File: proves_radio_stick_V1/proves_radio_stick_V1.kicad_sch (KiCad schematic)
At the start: 60 parts, among them J1 SWD Port, J12 USB_C_Receptacle_USB2.0_16P, J2 Conn_Coaxial, J22 SWD Port, SW1 KMR2, SW2 KMR2, U11 W25Q128JVS, U18 RP2350_60QFN, U2 TPS62085RLTT, U3 E32-400M20S_C2965514, Y1 ABM8-272-T3

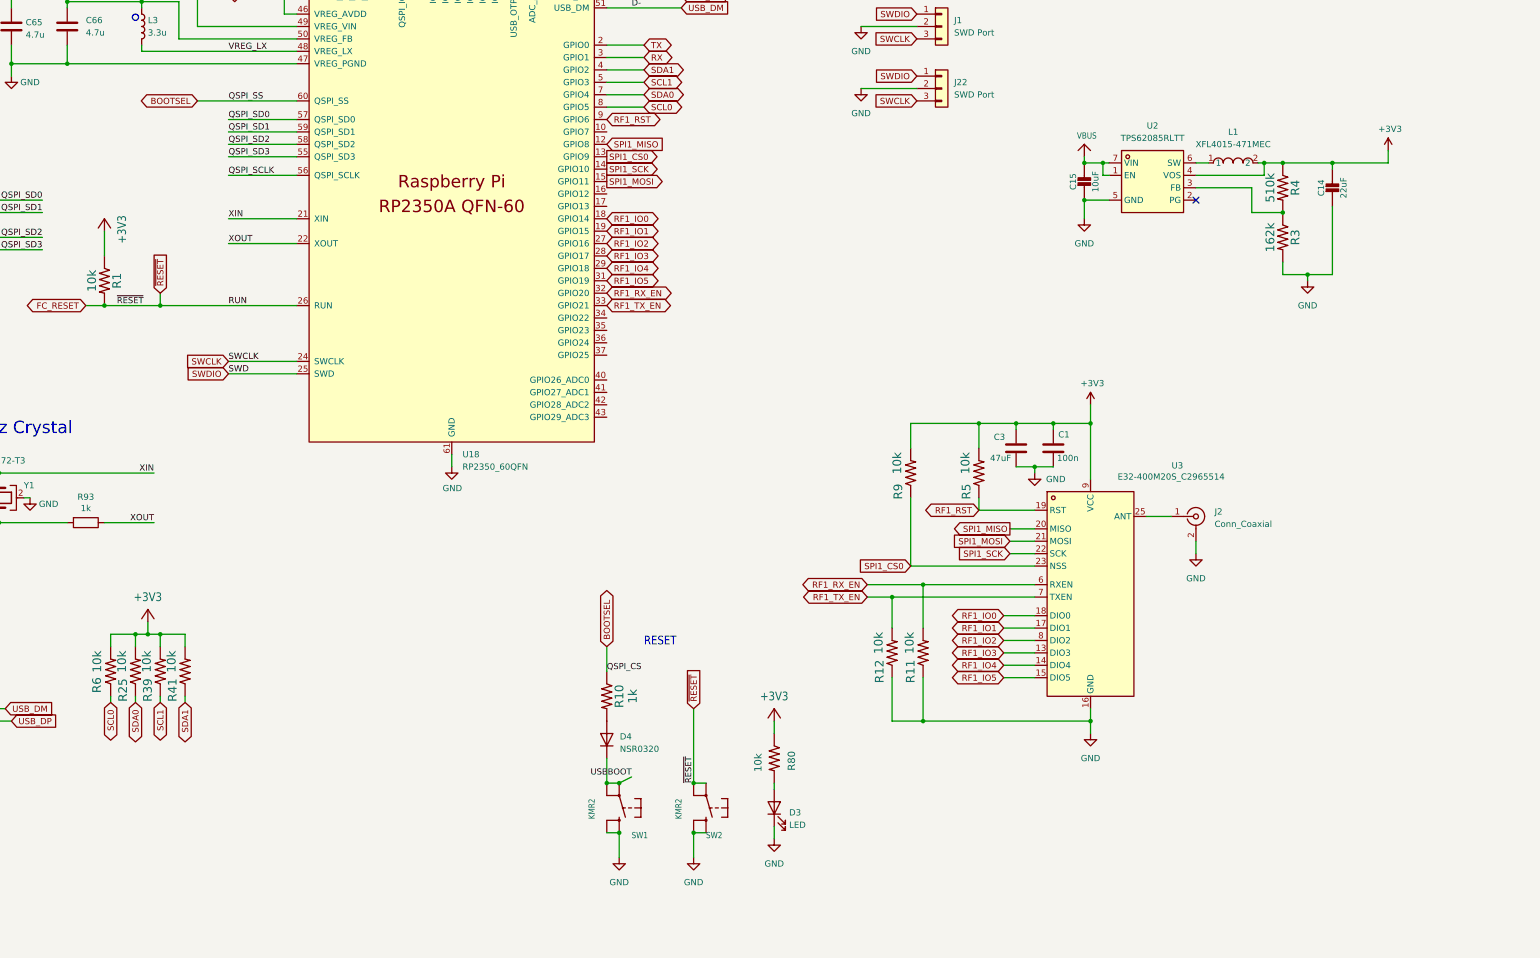
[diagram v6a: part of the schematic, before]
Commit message: Updated with Screw Terminals and Vias
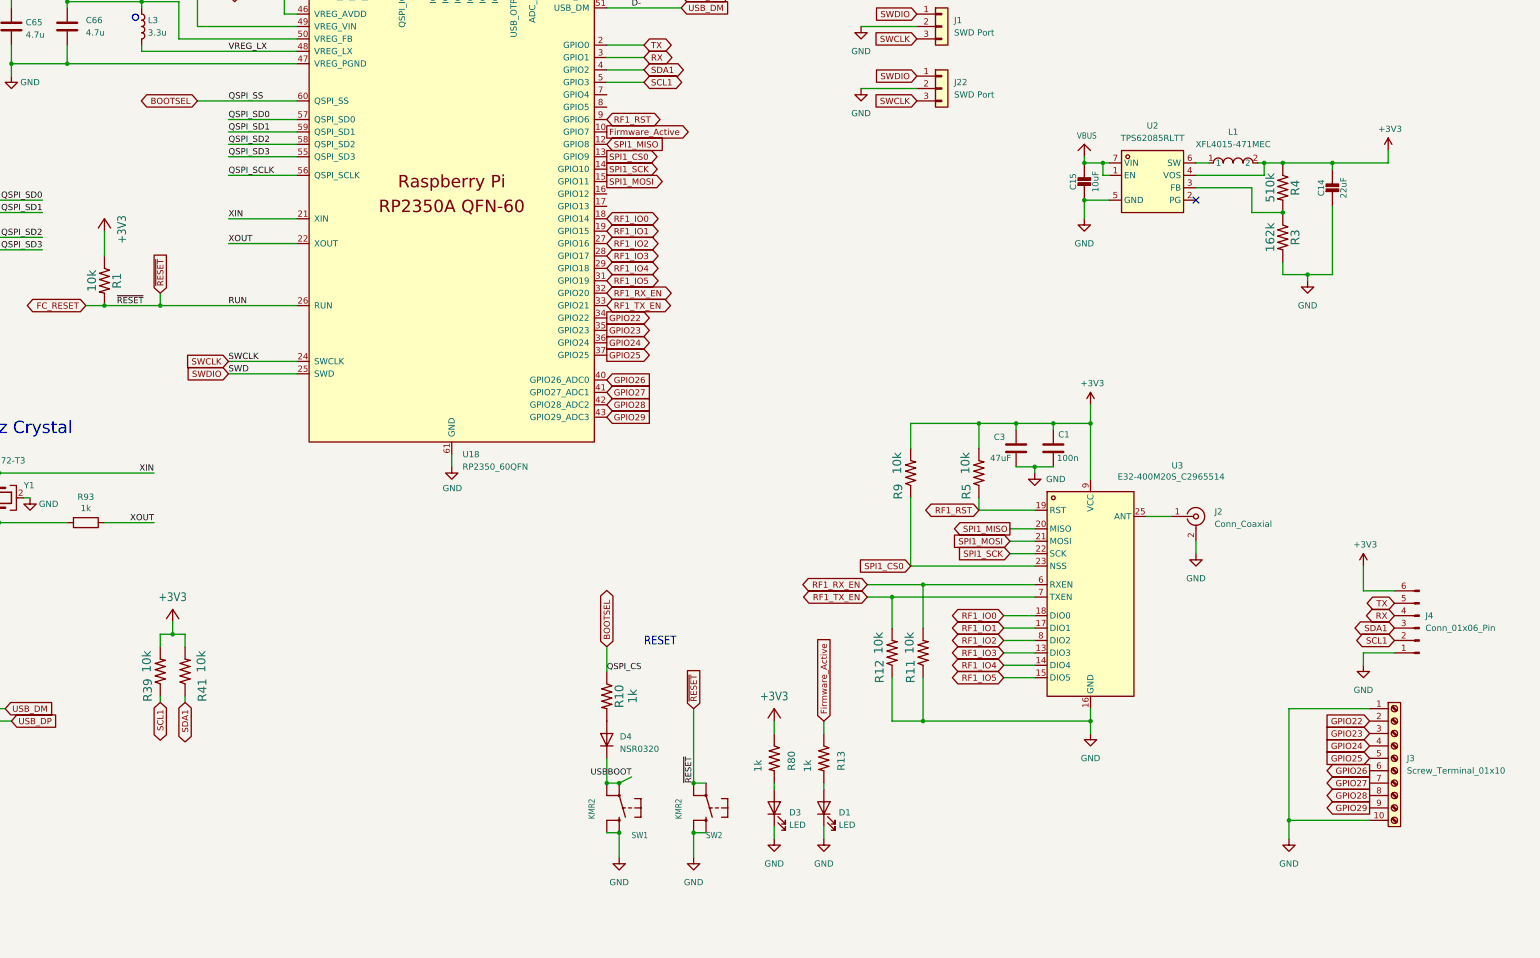
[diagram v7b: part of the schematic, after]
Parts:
- removed R25, R6: 10k, Resistor_SMD:R_0402_1005Metric, symbol mainboard:RESISTOR0603
- added D1: LED, LED_SMD:LED_0603_1608Metric, symbol Device:LED
- added J3: Screw_Terminal_01x10, TerminalBlock_Phoenix:TerminalBlock_Phoenix_MPT-0,5-10-2.54_1x10_P2.54mm_Horizontal, symbol Connector:Screw_Terminal_01x10
- added J4: Conn_01x06_Pin, Connector_PinHeader_2.54mm:PinHeader_1x06_P2.54mm_Vertical, symbol Connector:Conn_01x06_Pin
- added R13: 1k, Resistor_SMD:R_0402_1005Metric, symbol mainboard:R-US_R0603
- H1: footprint MountingHole:MountingHole_2.2mm_M2_Pad_Via -> MountingHole:MountingHole_2.2mm_M2_Pad_TopBottom
- R80: value 10k -> 1k
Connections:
- net +3V3: now also J4.6 (Pin_6)
- net GND: now also D1.1 (K), J3.1 (Pin_1), J3.10 (Pin_10), J4.1 (Pin_1)
- net RX: now also J4.4 (Pin_4)
- net SCL1: now also J4.2 (Pin_2)
- net SDA1: now also J4.3 (Pin_3)
- net TX: now also J4.5 (Pin_5)
- net Firmware_Active: now reaches U18.10 (GPIO7)
- net Firmware_Active: now also R13.1
- net GPIO22: now reaches U18.34 (GPIO22)
- net GPIO22: now also J3.2 (Pin_2)
- net GPIO23: now reaches U18.35 (GPIO23)
- net GPIO23: now also J3.3 (Pin_3)
- net GPIO24: now reaches U18.36 (GPIO24)
- net GPIO24: now also J3.4 (Pin_4)
- net GPIO25: now reaches U18.37 (GPIO25)
- net GPIO25: now also J3.5 (Pin_5)
- net GPIO26: now reaches U18.40 (GPIO26_ADC0)
- net GPIO26: now also J3.6 (Pin_6)
- net GPIO27: now reaches U18.41 (GPIO27_ADC1)
- net GPIO27: now also J3.7 (Pin_7)
- net GPIO28: now reaches U18.42 (GPIO28_ADC2)
- net GPIO28: now also J3.8 (Pin_8)
- net GPIO29: now reaches U18.43 (GPIO29_ADC3)
- net GPIO29: now also J3.9 (Pin_9)
- net SCL0: no longer names the net of U18.8 (GPIO5)
- net SDA0: no longer names the net of U18.7 (GPIO4)
- new net: D1.2 (A), R13.2

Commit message: Updated Prod Files
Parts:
- added TP1, TP2, TP3, TP4, TP5, TP6, TP7: TestPoint, TestPoint:TestPoint_Keystone_5000-5004_Miniature, symbol Connector:TestPoint
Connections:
- net RF1_IO0: now also TP5.1
- net RF1_IO1: now also TP6.1
- net RF1_RST: now also TP7.1
- net SPI1_CS0: now also TP2.1
- net SPI1_MISO: now also TP1.1
- net SPI1_MOSI: now also TP4.1
- net SPI1_SCK: now also TP3.1
- net SWCLK: now also J22.1 (Pin_1); no longer J22.3 (Pin_3)
- net SWDIO: now also J22.3 (Pin_3); no longer J22.1 (Pin_1)
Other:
- moved on the sheet: J1, J22
